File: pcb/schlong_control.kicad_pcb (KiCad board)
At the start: 2 copper layers, 88.9 x 80 mm, 46 parts, among them P1 Power Input (120V AC), P2 Power Thru (120V AC), P3 Input, P4 Output, U1 74HC595, U2 MOC3063M, U3 MOC3063M, U4 MOC3063M, U5 MOC3063M, U6 MOC3063M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

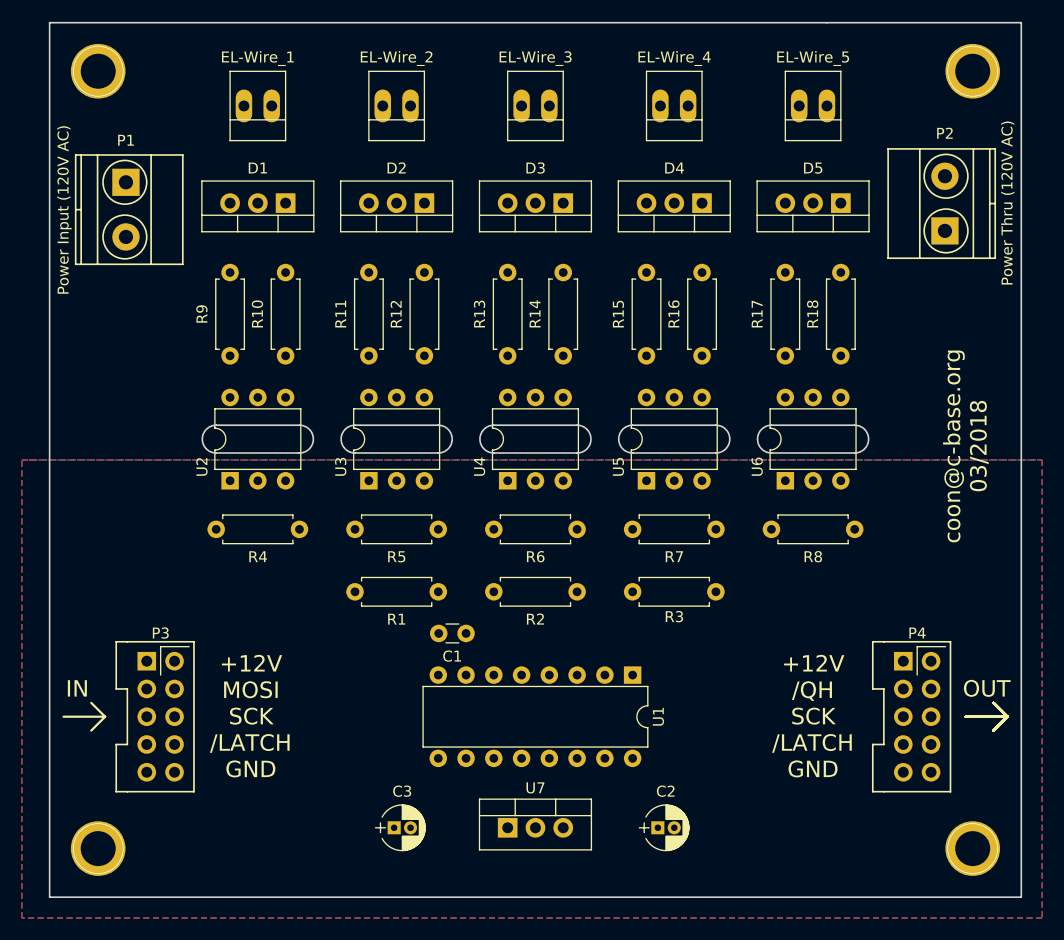
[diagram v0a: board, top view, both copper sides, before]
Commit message: pcb: finished rerouting
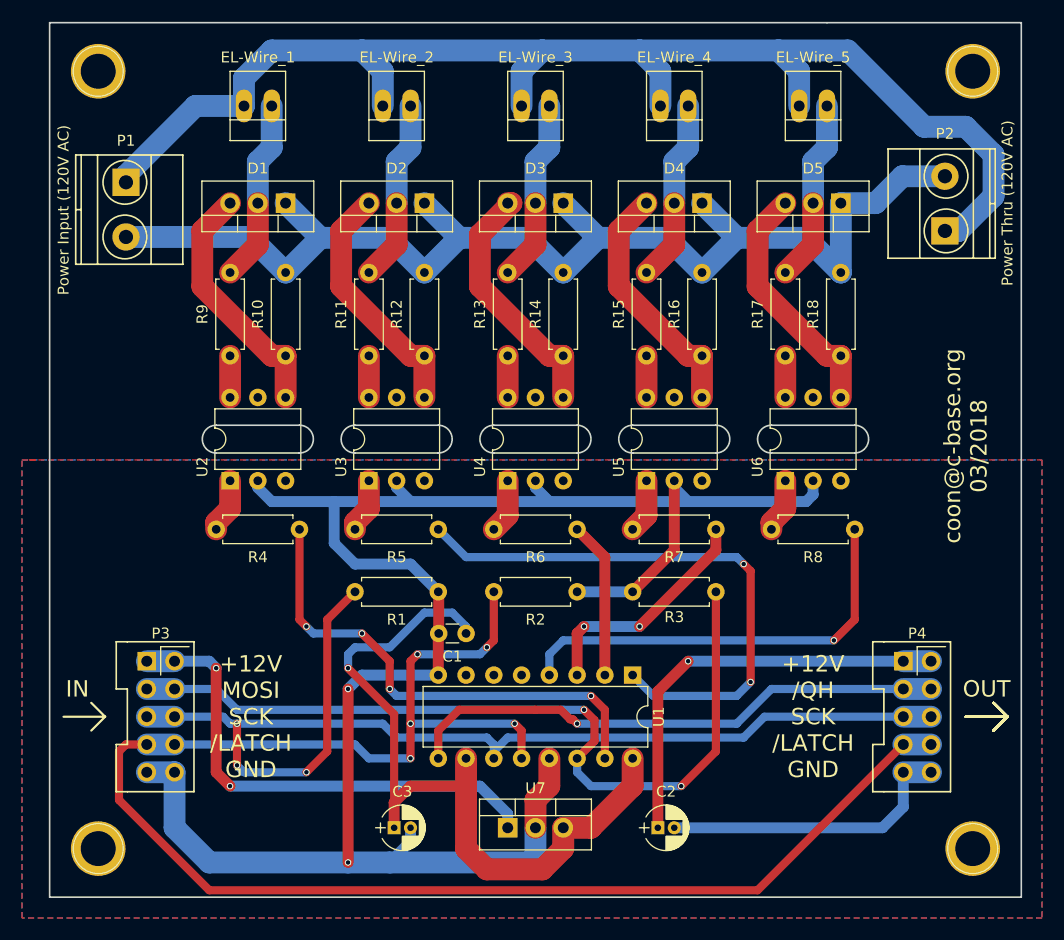
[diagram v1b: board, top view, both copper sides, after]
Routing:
- net GND: track 0.00 -> 217.2 mm, vias 0 -> 2
- net /~LATCH: track 0.00 -> 149.8 mm, vias 0 -> 5
- net /AC_P: track 0.00 -> 123.2 mm
- net /AC_N: track 0.00 -> 112.1 mm
- net /SCK: track 0.00 -> 104.8 mm, vias 0 -> 3
- net +12V: track 0.00 -> 84.3 mm, vias 0 -> 3
- net /MOSI: track 0.00 -> 76.7 mm, vias 0 -> 2
- net VCC: track 0.00 -> 69.5 mm, vias 0 -> 1
- net Net-(R5-Pad2): track 0.00 -> 52.4 mm, vias 0 -> 3
- net /~QH: track 0.00 -> 50.3 mm, vias 0 -> 1
- net Net-(R4-Pad2): track 0.00 -> 45.5 mm, vias 0 -> 4
- net Net-(R8-Pad2): track 0.00 -> 39.4 mm, vias 0 -> 1
- net Net-(D3-Pad3): track 0.00 -> 23.2 mm
- net Net-(D2-Pad3): track 0.00 -> 22.7 mm
- net Net-(D5-Pad3): track 0.00 -> 22.7 mm
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
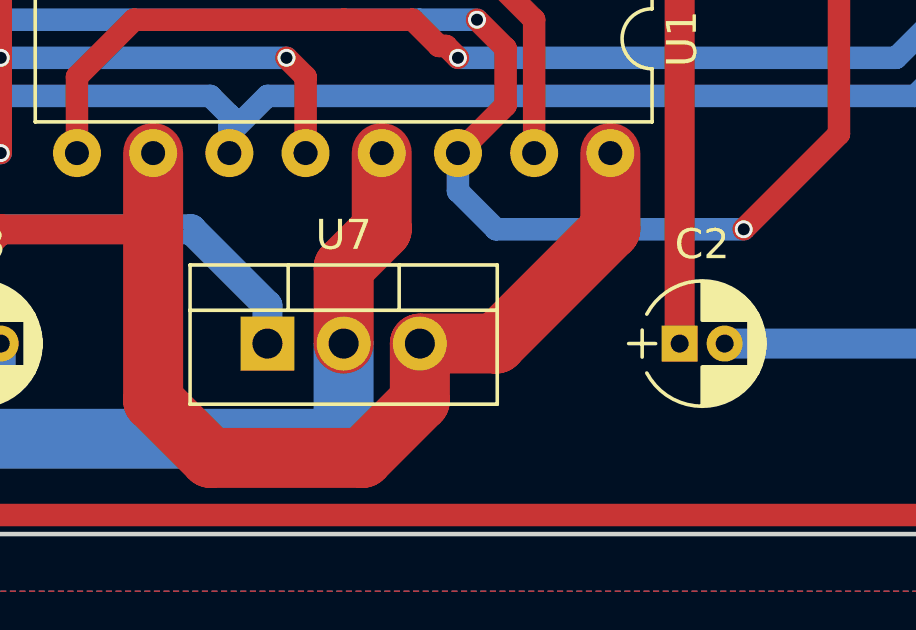
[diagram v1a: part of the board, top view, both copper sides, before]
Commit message: pcb: fix unconnected pad
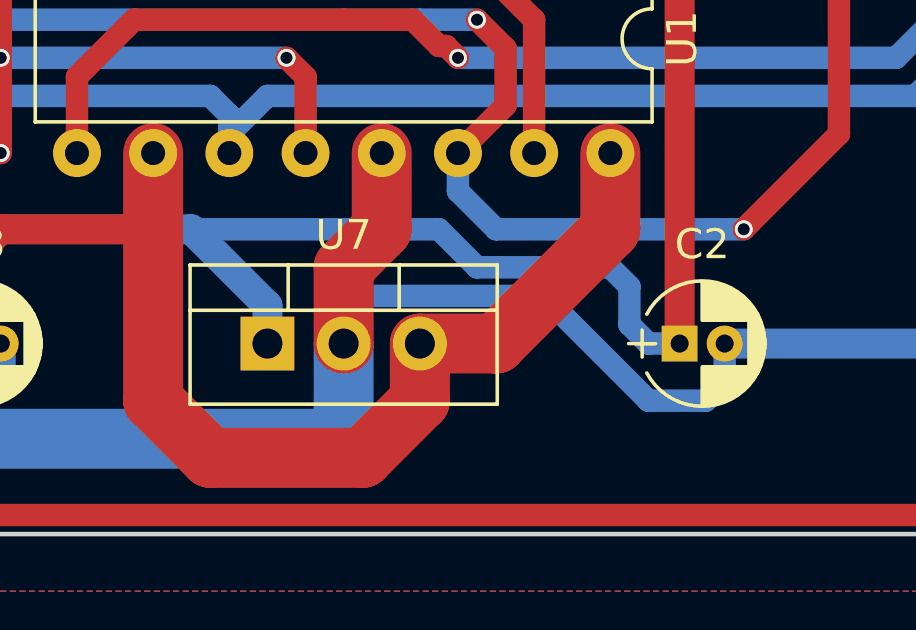
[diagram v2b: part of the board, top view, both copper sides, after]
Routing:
- net +12V: track 84.3 -> 102.9 mm
- net GND: track 217.2 -> 234.3 mm
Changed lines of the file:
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@@
   (general
     (links 93)
-    (no_connects 1)
+    (no_connects 0)
     (area 50.724999 25.324999 139.775001 105.485001)
     (thickness 1.6)
     (drawings 99)
-    (tracks 318)
+    (tracks 332)
     (zones 0)
     (modules 46)
@@
   (segment (start 104.14 95.25) (end 104.14 92.71) (width 2) (layer F.Cu) (net 1))
   (segment (start 100.33 99.06) (end 104.14 95.25) (width 2) (layer F.Cu) (net 1))
+  (segment (start 95.25 99.06) (end 95.25 97.79) (width 0.75) (layer B.Cu) (net 2))
+  (segment (start 107.95 100.33) (end 107.95 99.06) (width 0.75) (layer B.Cu) (net 2))
+  (segment (start 107.315 100.965) (end 107.95 100.33) (width 0.75) (layer B.Cu) (net 2))
+  (segment (start 105.41 100.965) (end 107.315 100.965) (width 0.75) (layer B.Cu) (net 2))
+  (segment (start 101.915002 97.470002) (end 105.41 100.965) (width 0.75) (layer B.Cu) (net 2))
+  (segment (start 95.569998 97.470002) (end 101.915002 97.470002) (width 0.75) (layer B.Cu) (net 2))
+  (segment (start 95.25 97.79) (end 95.569998 97.470002) (width 0.75) (layer B.Cu) (net 2))
   (segment (start 76.835 69.215) (end 76.835 73.025) (width 1) (layer B.Cu) (net 2))
   (segment (start 83.82 74.93) (end 86.36 77.47) (width 1) (layer B.Cu) (net 2))
@@
   (segment (start 107.95 67.945) (end 109.22 69.215) (width 1) (layer B.Cu) (net 2))
   (segment (start 128.905 93.98) (end 128.905 97.155) (width 1) (layer B.Cu) (net 2))
+  (segment (start 128.905 97.155) (end 127 99.06) (width 1) (layer B.Cu) (net 2))
   (segment (start 127 99.06) (end 107.95 99.06) (width 1) (layer B.Cu) (net 2))
-  (segment (start 128.905 97.155) (end 127 99.06) (width 1) (layer B.Cu) (net 2))
   (segment (start 62.23 99.06) (end 62.23 93.98) (width 1) (layer B.Cu) (net 2))
   (segment (start 64.77 101.6) (end 62.23 99.06) (width 1) (layer B.Cu) (net 2))
@@
   (segment (start 128.905 93.98) (end 131.445 93.98) (width 2) (layer B.Cu) (net 2))
   (segment (start 59.69 93.98) (end 62.23 93.98) (width 2) (layer B.Cu) (net 2))
+  (segment (start 90.17 95.25) (end 98.425 95.25) (width 0.75) (layer B.Cu) (net 3))
+  (segment (start 105.41 99.06) (end 106.45 99.06) (width 0.75) (layer B.Cu) (net 3))
+  (segment (start 104.775 98.425) (end 105.41 99.06) (width 0.75) (layer B.Cu) (net 3))
+  (segment (start 104.775 97.155) (end 104.775 98.425) (width 0.75) (layer B.Cu) (net 3))
+  (segment (start 104.14 96.52) (end 104.775 97.155) (width 0.75) (layer B.Cu) (net 3))
+  (segment (start 99.695 96.52) (end 104.14 96.52) (width 0.75) (layer B.Cu) (net 3))
+  (segment (start 98.425 95.25) (end 99.695 96.52) (width 0.75) (layer B.Cu) (net 3))
   (segment (start 106.45 99.06) (end 106.45 86.59) (width 1) (layer F.Cu) (net 3))
   (segment (start 109.22 83.82) (end 128.905 83.82) (width 1) (layer B.Cu) (net 3))
@@
   (segment (start 99.06 93.98) (end 100.33 95.25) (width 0.75) (layer B.Cu) (net 16))
   (segment (start 59.69 86.36) (end 62.23 86.36) (width 2) (layer B.Cu) (net 16))
-  (segment (start 91.44 92.71) (end 91.44 92.075) (width 0.75) (layer B.Cu) (net 17))
-  (segment (start 91.44 92.075) (end 92.71 90.805) (width 0.75) (layer B.Cu) (net 17))
   (segment (start 116.205 88.9) (end 128.905 88.9) (width 0.75) (layer B.Cu) (net 17))
   (segment (start 114.3 90.805) (end 116.205 88.9) (width 0.75) (layer B.Cu) (net 17))
   (segment (start 92.71 90.805) (end 114.3 90.805) (width 0.75) (layer B.Cu) (net 17))
+  (segment (start 91.44 92.075) (end 92.71 90.805) (width 0.75) (layer B.Cu) (net 17))
+  (segment (start 91.44 92.71) (end 91.44 92.075) (width 0.75) (layer B.Cu) (net 17))
   (segment (start 67.31 89.535) (end 67.945 89.535) (width 0.75) (layer B.Cu) (net 17))
   (segment (start 67.945 89.535) (end 81.28 89.535) (width 0.75) (layer B.Cu) (net 17))

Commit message: pcb: update gerber files
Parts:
- P3: footprint idc:IDC_Header_Straight_2x05_Pitch2.54mm -> idc:IDC_Header_Straight_2x05_Pitch2.54mm_Mirrored
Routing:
- net GND: track 234.3 -> 232.3 mm
